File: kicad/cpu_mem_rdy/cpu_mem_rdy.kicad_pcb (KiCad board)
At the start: 2 copper layers, 160 x 100.3 mm, 68 parts, among them CON1 USB-MICRO-B, P1 CONN_02X04, P2 CONN_01X08, P3 CONN_01X03, P4 CONN_02X02, P5 CONN_02X25, P6 POWER, SW1 RESET, U1 65C02, U11 74HCT273, U12 74HCT244, U14 GAL16V8, U2 NE555, U3 74HCT00, U4 74HCT393, U5 GAL22V10, U6 28C256, U7 62256, U8 62256, U9 74HCT139, X1 OSC

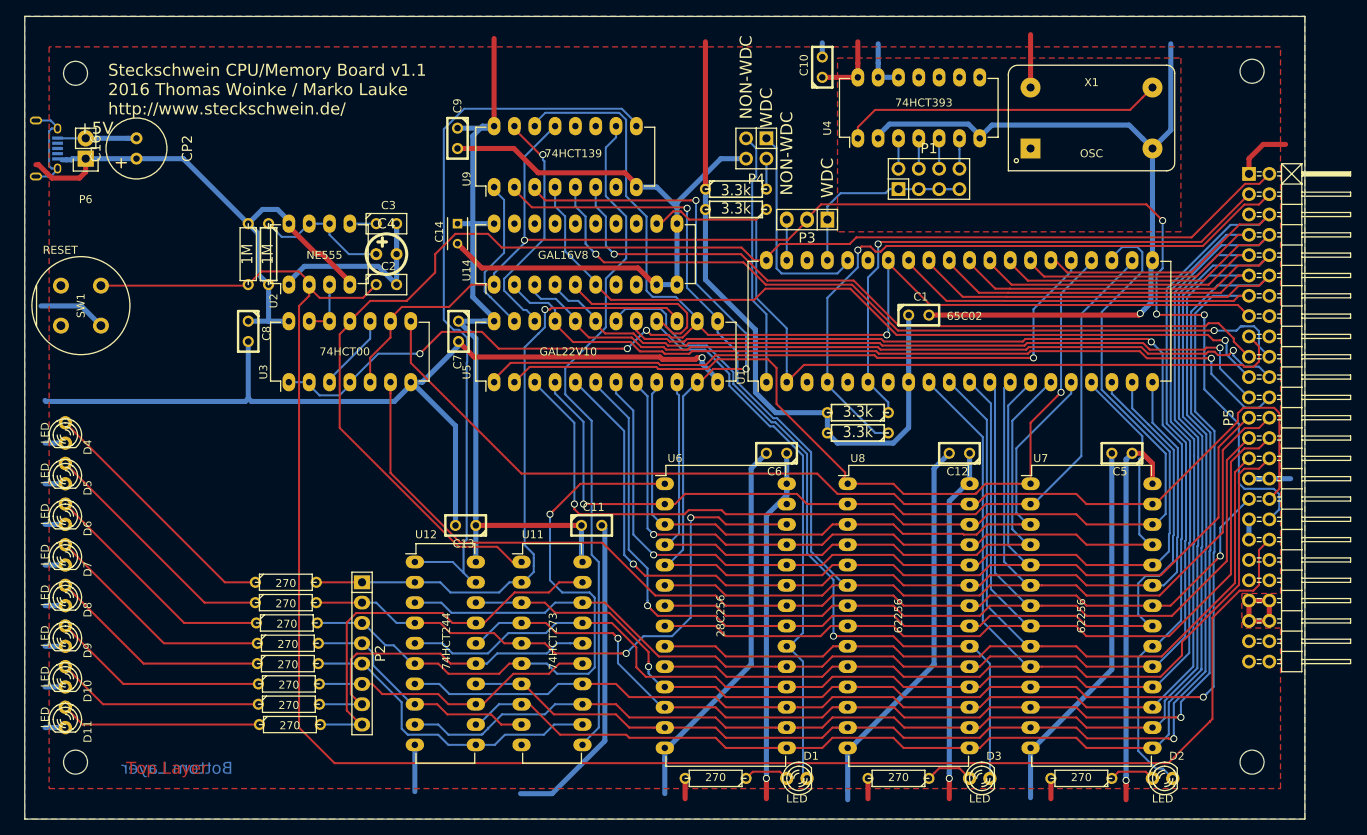
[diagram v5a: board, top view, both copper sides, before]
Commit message: no rdy for via, io1-3 connected to rdygen
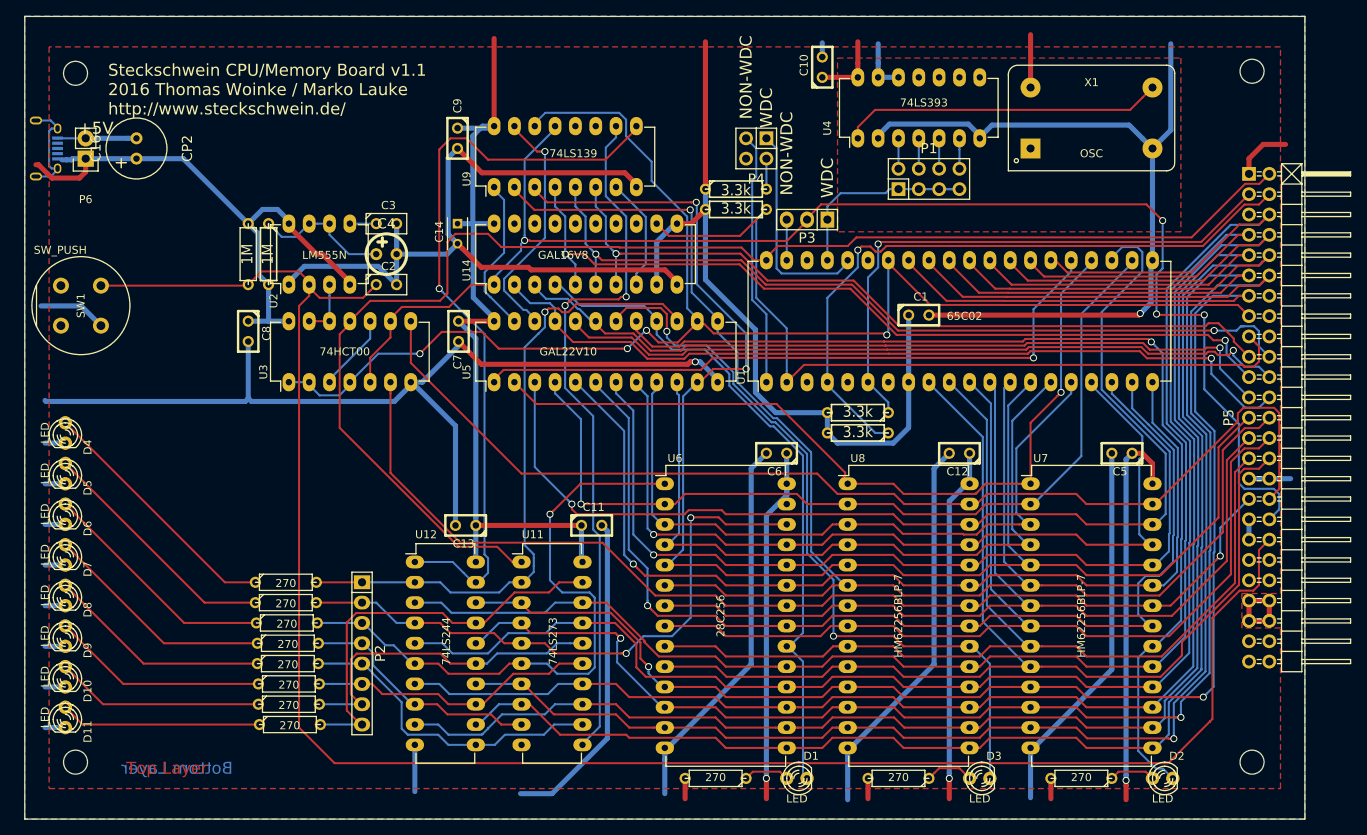
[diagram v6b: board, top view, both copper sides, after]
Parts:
- SW1: value RESET -> SW_PUSH
- U11: value 74HCT273 -> 74LS273
- U12: value 74HCT244 -> 74LS244
- U2: value NE555 -> LM555N
- U4: value 74HCT393 -> 74LS393
- U7, U8: value 62256 -> HM62256BLP-7
- U9: value 74HCT139 -> 74LS139
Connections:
- U14 pad 11: GND -> VCC
- U14 pad 3: /CS_VIA -> /CS_UART
- U14 pad 4: /CS_UART -> /decoder//CS_ROM
- U14 pad 5: /decoder//CS_ROM -> /CS_IO0
- U14 pad 6: /CS_IO0 -> /CS_IO1
- U14 pad 7: Net-(U14-Pad7) -> /CS_IO2
- U14 pad 8: Net-(U14-Pad8) -> /decoder//CS_IO3
- U14 pad 9: GND -> VCC
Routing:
- net /decoder//CS_IO3: track 0.00 -> 14.2 mm
- net VCC: track 440.0 -> 452.0 mm
- net /CS_VIA: track 99.2 -> 92.0 mm
- net GND: track 572.3 -> 566.1 mm
- net /decoder//CS_ROM: track 91.5 -> 85.7 mm
- net /decoder/A14: track 108.8 -> 103.6 mm
- net /CS_IO1: track 100.9 -> 105.1 mm
- net Net-(U11-Pad11): track 84.7 -> 88.7 mm, vias 0 -> 2
- net /CS_IO0: track 102.9 -> 106.7 mm, vias 1 -> 2
- net /CS_IO2: track 94.5 -> 98.2 mm
- net /CS_UART: track 95.6 -> 98.6 mm
- net Net-(U12-Pad1): track 92.5 -> 95.1 mm, vias 0 -> 1
- net /RESET: track 171.1 -> 173.6 mm
- net /decoder//CS_HIRAM: track 93.4 -> 94.7 mm, vias 1 -> 2
- net /RW: track 184.8 -> 183.6 mm
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
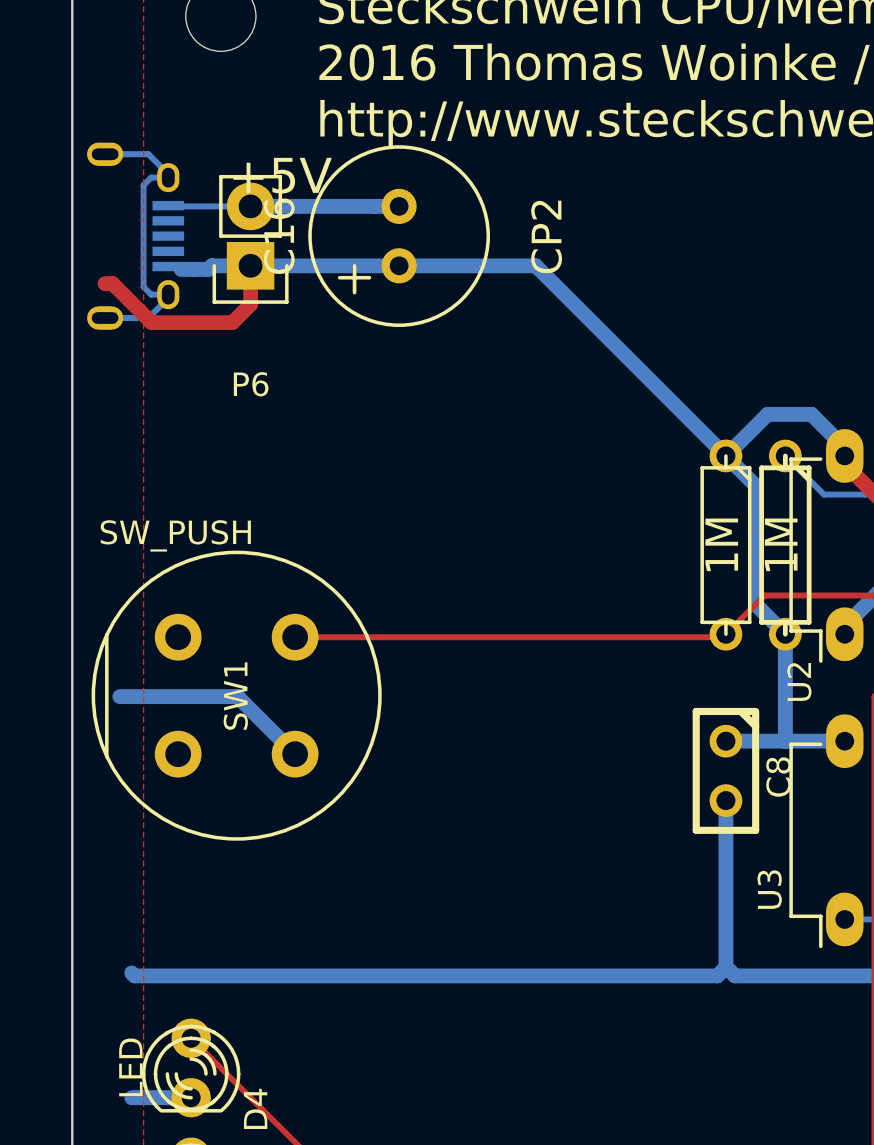
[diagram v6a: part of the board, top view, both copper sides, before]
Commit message: USB B for power
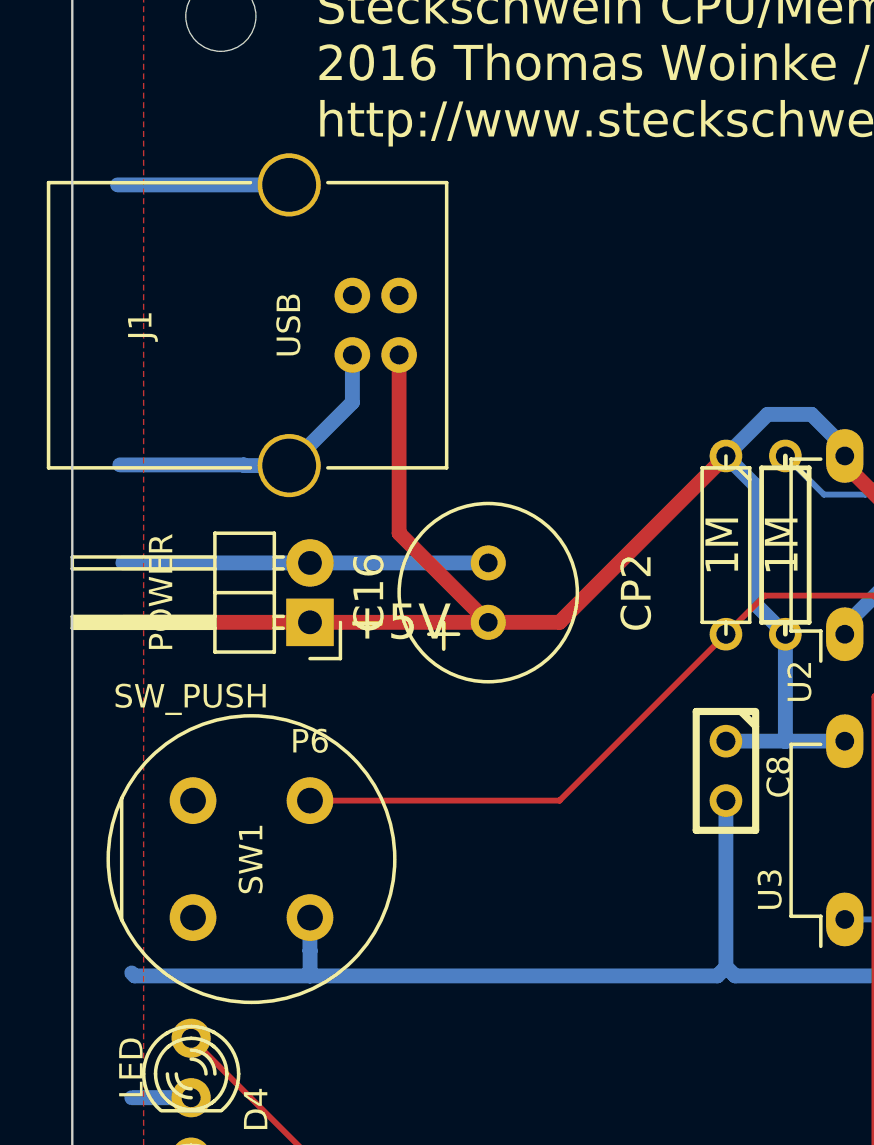
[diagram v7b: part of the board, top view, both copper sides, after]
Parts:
- removed CON1: USB-MICRO-B, Connect:USB_Micro-B
- added J1: USB, Connect:USB_B, F.Cu at (76.2, 67.3)
- P6: footprint Pin_Headers:Pin_Header_Straight_1x02 -> Pin_Headers:Pin_Header_Angled_1x02
- moved C16 15.7 mm to (80.0, 78.7)
- moved P6 15.5 mm to (72.4, 78.7)
- moved SW1 7.01 mm to (72.4, 86.4)
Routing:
- net GND: track 566.1 -> 586.3 mm
- net Net-(CON1-Pad6): track 13.1 -> 0.00 mm
- net VCC: track 452.0 -> 458.1 mm
- net /Connector/RESET_TRIG: track 238.2 -> 240.7 mm

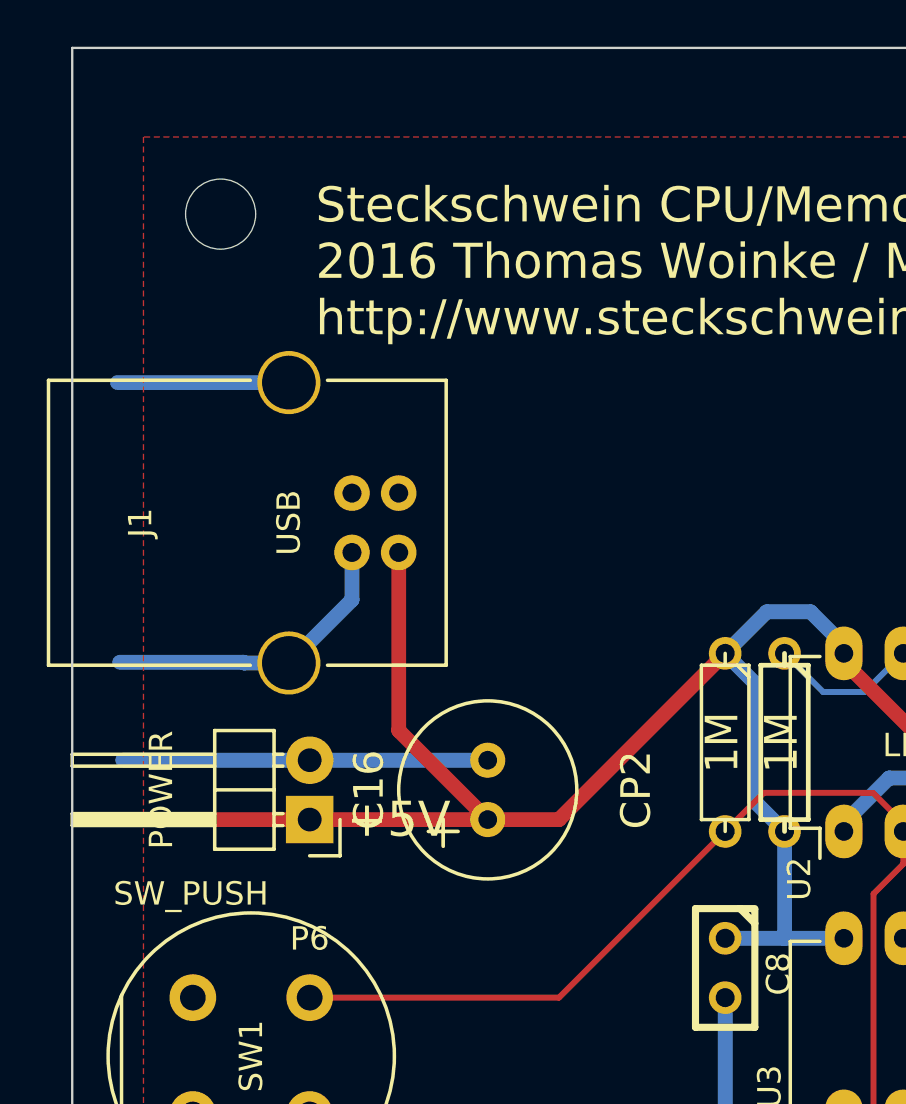
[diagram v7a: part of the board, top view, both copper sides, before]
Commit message: barrel jack
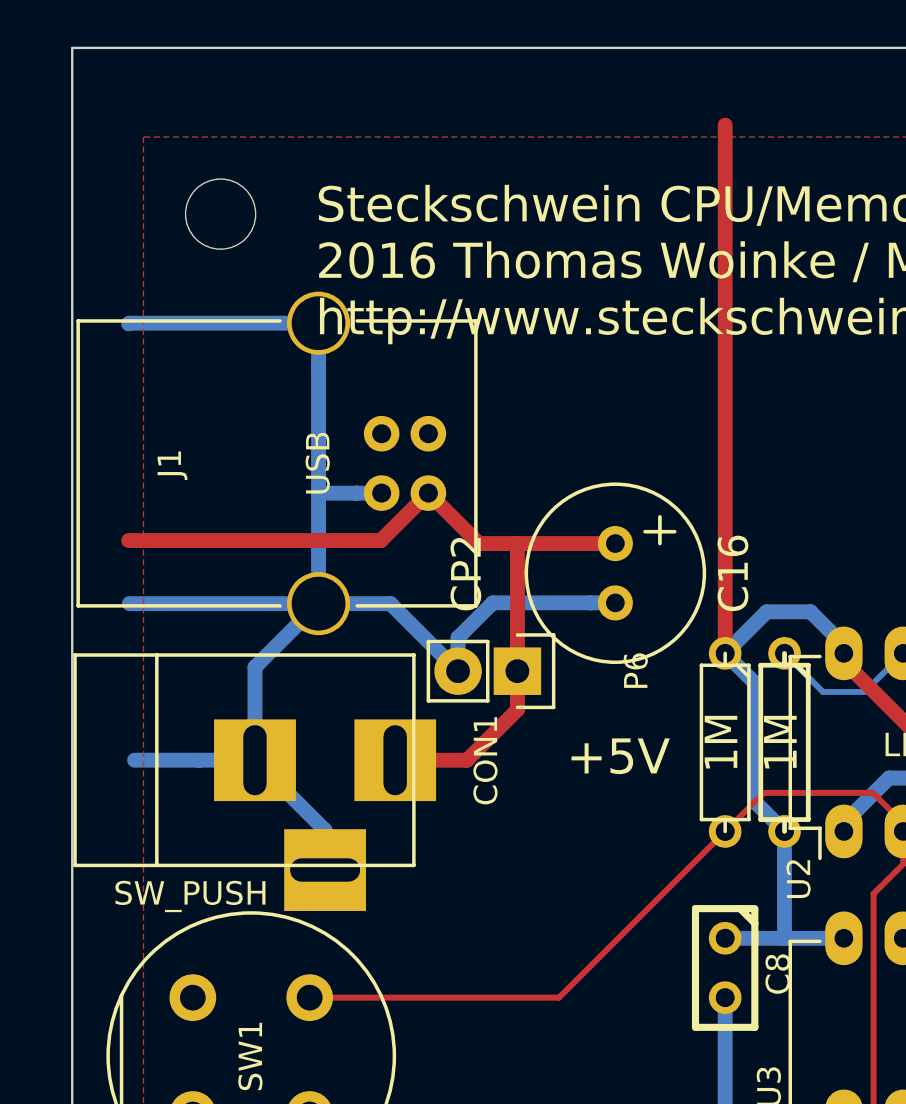
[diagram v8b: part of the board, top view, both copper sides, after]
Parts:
- added CON1: BARREL_JACK, Connect:BARREL_JACK, F.Cu at (69.8, 76.2)
- P6: footprint Pin_Headers:Pin_Header_Angled_1x02 -> Pin_Headers:Pin_Header_Straight_1x02
- moved C16 13.0 mm to (85.5, 66.9), turned to 270 degrees
- moved P6 10.9 mm to (81.3, 72.4), turned to 270 degrees
- moved J1 2.84 mm to (77.5, 64.8)
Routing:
- net GND: track 586.3 -> 616.1 mm
- net VCC: track 458.1 -> 474.8 mm
